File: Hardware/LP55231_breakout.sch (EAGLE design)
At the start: 29 parts, among them J1 To micro, J2 USER LED, J3 USER LED, J4 USER LED, U1 LP55231WQFN

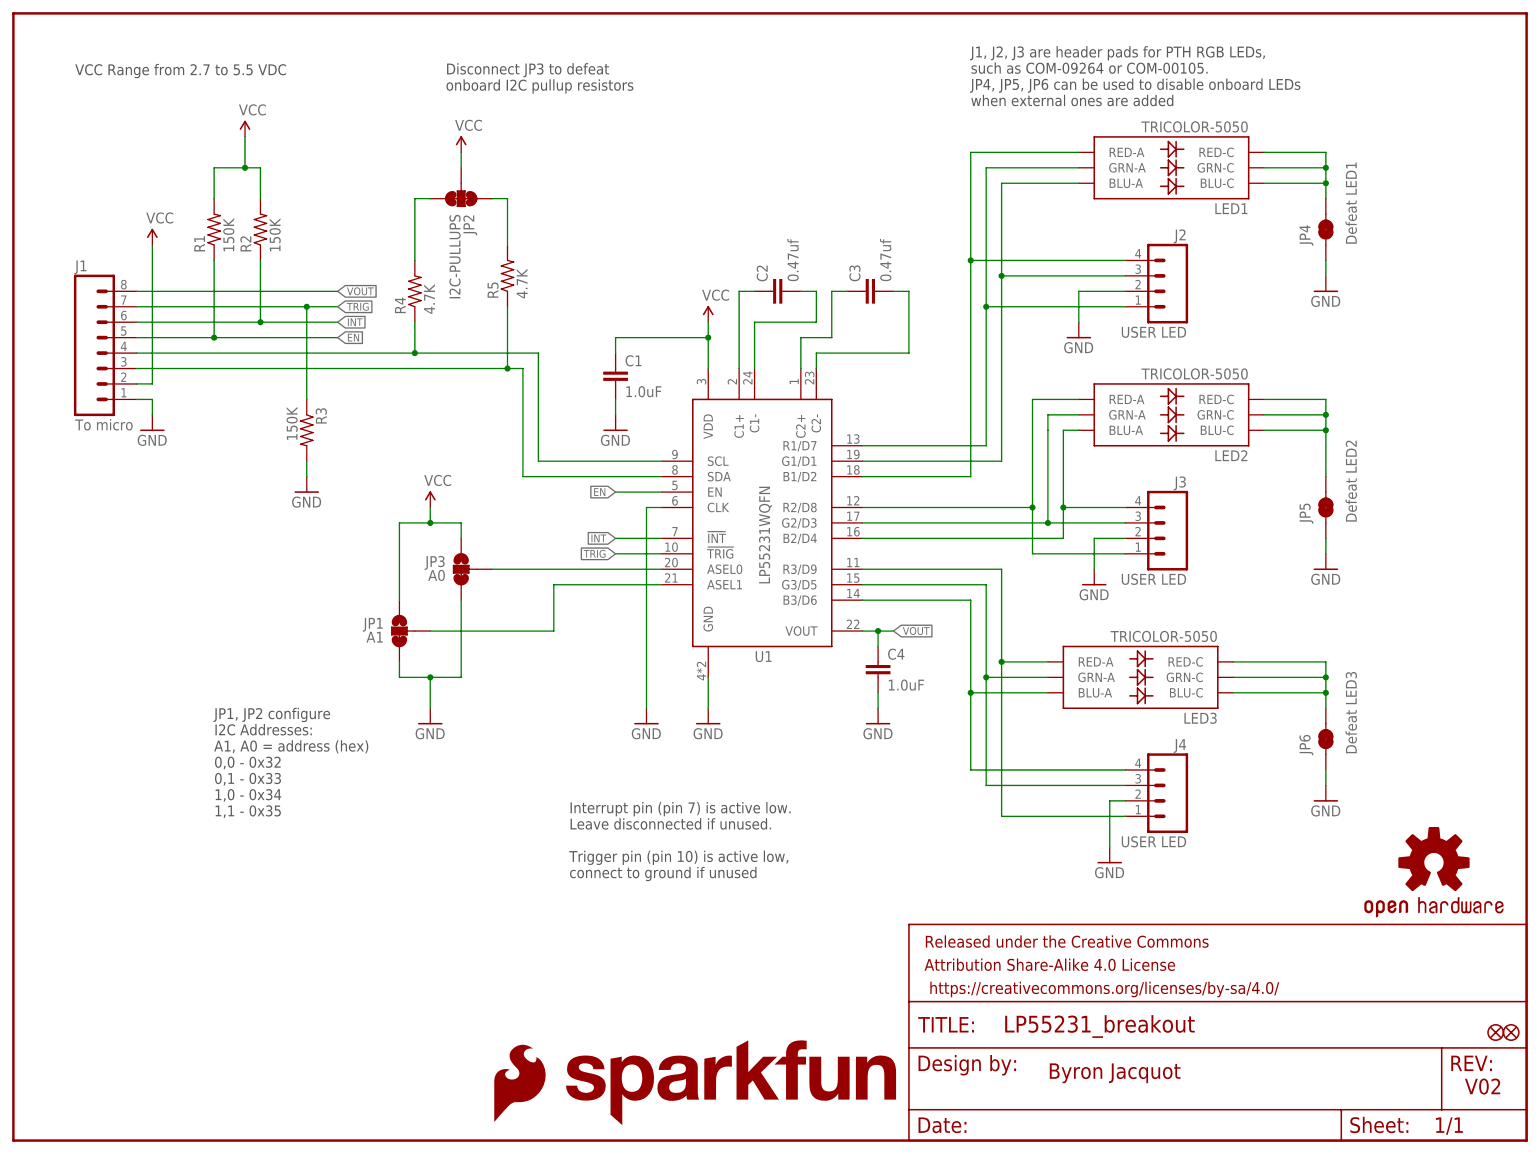
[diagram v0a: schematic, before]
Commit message: Checklist review issues
Numbering of jumpers vs. comments got mismatched.
Now fixed.
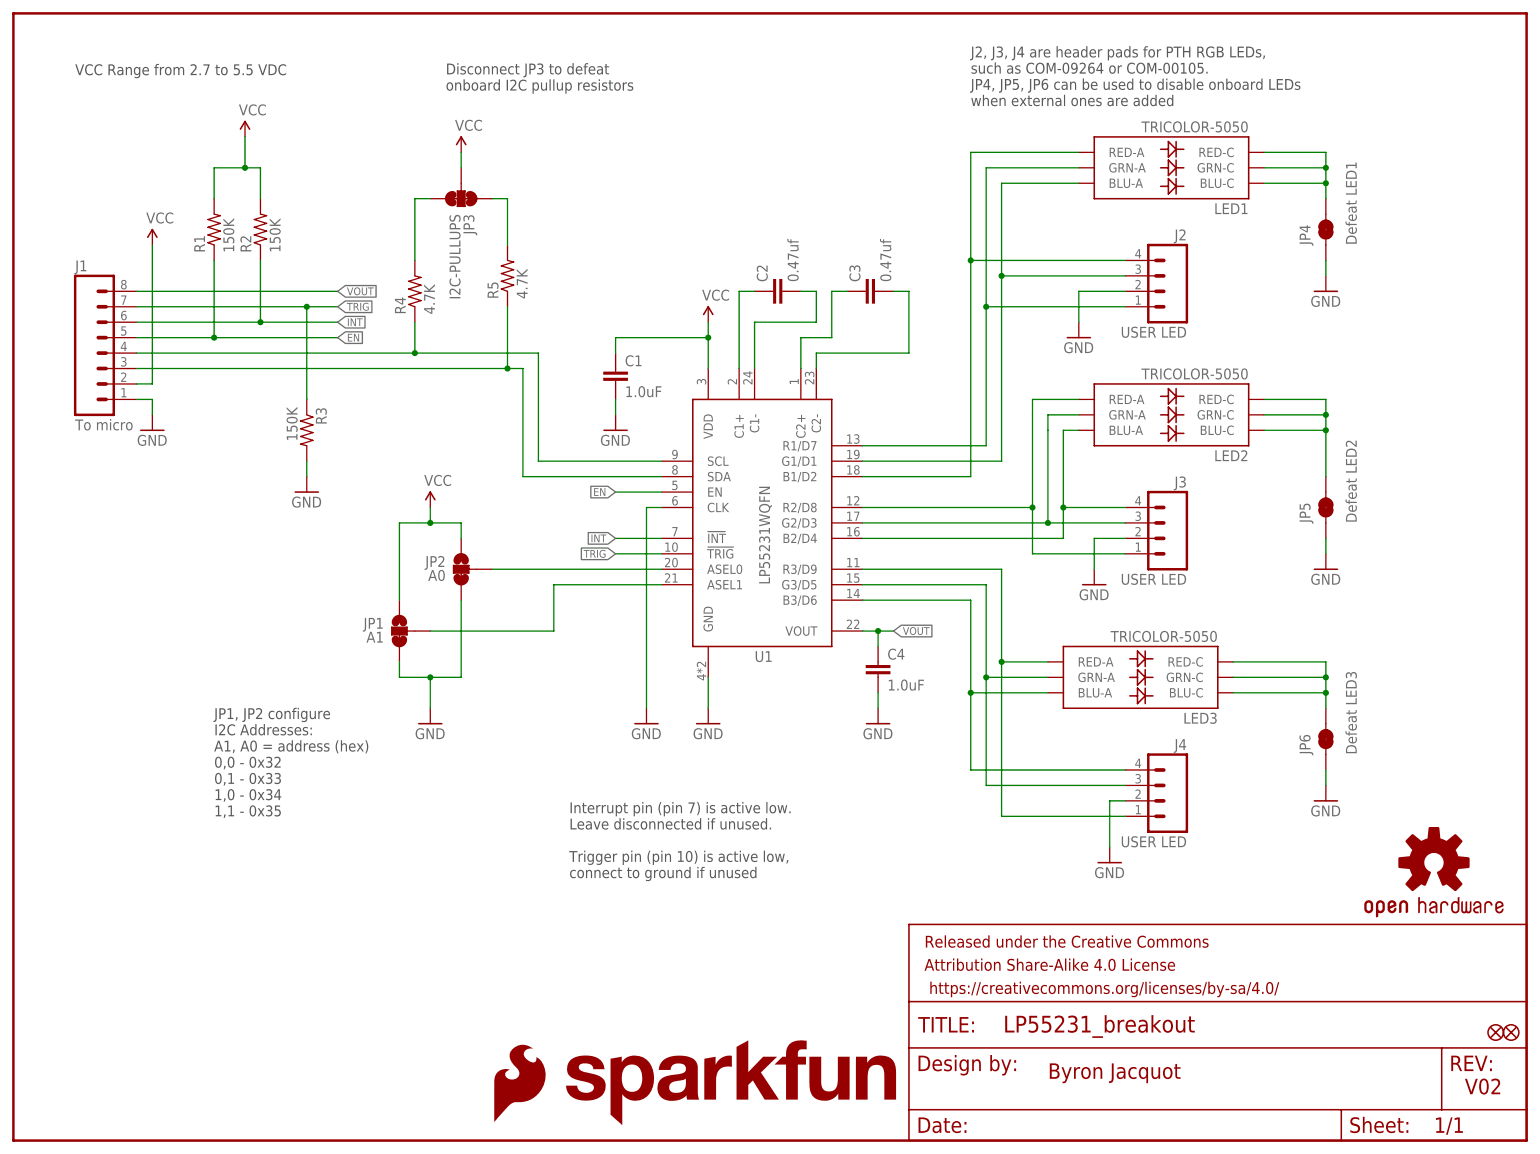
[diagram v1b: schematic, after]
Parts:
- JP2: value I2C-PULLUPS -> A0; device SparkFun-Passives:JUMPER-PAD-3-NC_BY_TRACE -> SparkFun-Passives:JUMPER-PAD-3-2OF3_NC_BY_TRACE_SMALL
- JP3: value A0 -> I2C-PULLUPS; device SparkFun-Passives:JUMPER-PAD-3-2OF3_NC_BY_TRACE_SMALL -> SparkFun-Passives:JUMPER-PAD-3-NC_BY_TRACE
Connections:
- net ADDR0: now also JP2.2; no longer JP3.2
- net GND: now also JP2.3; no longer JP3.3
- net N$21: now also JP3.1; no longer JP2.1
- net N$22: now also JP3.3; no longer JP2.3
- net VCC: now also JP2.1, JP3.2; no longer JP2.2, JP3.1
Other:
- note added: "J2, J3, J4 are header pads for PTH RGB LEDs, such as COM-09264 or COM-00105. JP4, JP5, JP6 can be used to disable onboard LEDs when external ones are added"
- note removed: "J1, J2, J3 are header pads for PTH RGB LEDs, such as COM-09264 or COM-00105. JP4, JP5, JP6 can be used to disable onboard LEDs when external ones are added"
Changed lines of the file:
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@@
 <attribute name="SEE-ALSO" value="battery bayasitter"/>
 </part>
-<part name="JP3" library="SparkFun-Passives" deviceset="JUMPER-PAD-3-2OF3_NC_BY_TRACE" device="_SMALL" value="A0"/>
+<part name="JP2" library="SparkFun-Passives" deviceset="JUMPER-PAD-3-2OF3_NC_BY_TRACE" device="_SMALL" value="A0"/>
 <part name="JP1" library="SparkFun-Passives" deviceset="JUMPER-PAD-3-2OF3_NC_BY_TRACE" device="_SMALL" value="A1"/>
 <part name="GND3" library="SparkFun-Aesthetics" deviceset="GND" device=""/>
@@
 <part name="GND1" library="SparkFun-Aesthetics" deviceset="GND" device=""/>
 <part name="SUPPLY1" library="SparkFun-Aesthetics" deviceset="VCC" device=""/>
-<part name="JP2" library="SparkFun-Passives" deviceset="JUMPER-PAD-3-NC_BY_TRACE" device="" value="I2C-PULLUPS"/>
+<part name="JP3" library="SparkFun-Passives" deviceset="JUMPER-PAD-3-NC_BY_TRACE" device="" value="I2C-PULLUPS"/>
 <part name="SUPPLY4" library="SparkFun-Aesthetics" deviceset="VCC" device=""/>
 <part name="R4" library="SparkFun-Resistors" deviceset="4.7KOHM-1/10W-1%(0603)" device="" value="4.7K"/>
@@
 1,0 - 0x34
 1,1 - 0x35</text>
-<text x="157.48" y="170.18" size="1.778" layer="97" font="vector">J1, J2, J3 are header pads for PTH RGB LEDs,
+<text x="157.48" y="170.18" size="1.778" layer="97" font="vector">J2, J3, J4 are header pads for PTH RGB LEDs,
 such as COM-09264 or COM-00105.
 JP4, JP5, JP6 can be used to disable onboard LEDs
@@
 <attribute name="SEE-ALSO" x="142.24" y="139.7" size="1.778" layer="96" font="vector" rot="R90" display="off"/>
 </instance>
-<instance part="JP3" gate="G$1" x="73.66" y="93.98" rot="MR0"/>
+<instance part="JP2" gate="G$1" x="73.66" y="93.98" rot="MR0"/>
 <instance part="JP1" gate="G$1" x="63.5" y="83.82" rot="MR0"/>
 <instance part="GND3" gate="1" x="68.58" y="68.58"/>
@@
 <instance part="GND1" gate="1" x="22.86" y="116.84"/>
 <instance part="SUPPLY1" gate="G$1" x="22.86" y="147.32"/>
-<instance part="JP2" gate="G$1" x="73.66" y="154.94" rot="R270"/>
+<instance part="JP3" gate="G$1" x="73.66" y="154.94" rot="R270"/>
 <instance part="SUPPLY4" gate="G$1" x="73.66" y="162.56"/>
 <instance part="R4" gate="G$1" x="66.04" y="139.7" rot="R90"/>
@@
 <pinref part="JP1" gate="G$1" pin="3"/>
 <wire x1="63.5" y1="76.2" x2="63.5" y2="78.74" width="0.1524" layer="91"/>
-<pinref part="JP3" gate="G$1" pin="3"/>
+<pinref part="JP2" gate="G$1" pin="3"/>
 <wire x1="73.66" y1="88.9" x2="73.66" y2="76.2" width="0.1524" layer="91"/>
 <wire x1="73.66" y1="76.2" x2="68.58" y2="76.2" width="0.1524" layer="91"/>
@@
 </segment>
 <segment>
-<pinref part="JP3" gate="G$1" pin="1"/>
+<pinref part="JP2" gate="G$1" pin="1"/>
 <wire x1="73.66" y1="99.06" x2="73.66" y2="101.6" width="0.1524" layer="91"/>
 <wire x1="73.66" y1="101.6" x2="68.58" y2="101.6" width="0.1524" layer="91"/>
@@
 <segment>
 <pinref part="SUPPLY4" gate="G$1" pin="VCC"/>
-<pinref part="JP2" gate="G$1" pin="2"/>
+<pinref part="JP3" gate="G$1" pin="2"/>
 <wire x1="73.66" y1="162.56" x2="73.66" y2="160.02" width="0.1524" layer="91"/>
 </segment>
@@
 <segment>
 <pinref part="U1" gate="G$1" pin="ASEL0"/>
-<pinref part="JP3" gate="G$1" pin="2"/>
+<pinref part="JP2" gate="G$1" pin="2"/>
 <wire x1="106.68" y1="93.98" x2="78.74" y2="93.98" width="0.1524" layer="91"/>
 </segment>
@@
 <pinref part="R5" gate="G$1" pin="2"/>
 <wire x1="81.28" y1="147.32" x2="81.28" y2="154.94" width="0.1524" layer="91"/>
-<pinref part="JP2" gate="G$1" pin="1"/>
+<pinref part="JP3" gate="G$1" pin="1"/>
 <wire x1="81.28" y1="154.94" x2="78.74" y2="154.94" width="0.1524" layer="91"/>
 </segment>
@@
 <pinref part="R4" gate="G$1" pin="2"/>
 <wire x1="66.04" y1="144.78" x2="66.04" y2="154.94" width="0.1524" layer="91"/>
-<pinref part="JP2" gate="G$1" pin="3"/>
+<pinref part="JP3" gate="G$1" pin="3"/>
 <wire x1="66.04" y1="154.94" x2="68.58" y2="154.94" width="0.1524" layer="91"/>
 </segment>

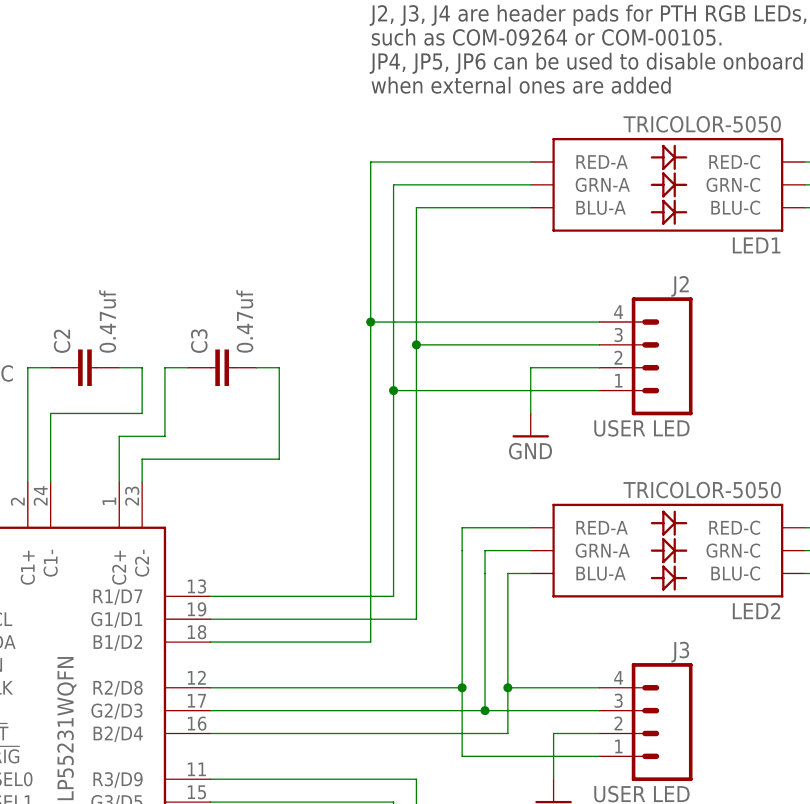
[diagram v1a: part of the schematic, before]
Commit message: Fixing RGB assignments of first LED.
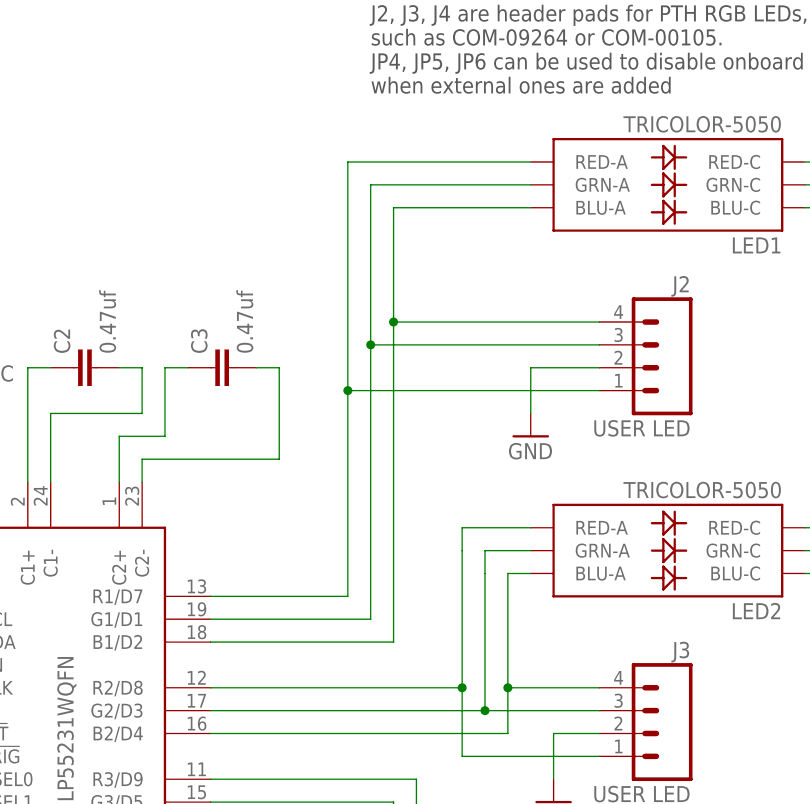
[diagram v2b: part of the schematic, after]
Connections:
- net B1: now also LED1.BLU-A; no longer LED1.RED-A
- net G1: now also LED1.GRN-A; no longer LED1.BLU-A
- net R1: now also LED1.RED-A; no longer LED1.GRN-A
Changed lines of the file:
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@@
 <setting verticaltext="up"/>
 </settings>
-<grid distance="0.1" unitdist="inch" unit="inch" style="lines" multiple="1" display="no" altdistance="0.01" altunitdist="inch" altunit="inch"/>
+<grid distance="0.1" unitdist="inch" unit="inch" style="lines" multiple="1" display="yes" altdistance="0.01" altunitdist="inch" altunit="inch"/>
 <layers>
 <layer number="1" name="Top" color="4" fill="1" visible="no" active="no"/>
@@
 <segment>
 <pinref part="U1" gate="G$1" pin="R1/D7"/>
-<wire x1="139.7" y1="114.3" x2="160.02" y2="114.3" width="0.1524" layer="91"/>
-<wire x1="160.02" y1="114.3" x2="160.02" y2="137.16" width="0.1524" layer="91"/>
-<wire x1="160.02" y1="137.16" x2="160.02" y2="160.02" width="0.1524" layer="91"/>
-<wire x1="160.02" y1="160.02" x2="175.26" y2="160.02" width="0.1524" layer="91"/>
+<wire x1="139.7" y1="114.3" x2="154.94" y2="114.3" width="0.1524" layer="91"/>
+<wire x1="154.94" y1="114.3" x2="154.94" y2="137.16" width="0.1524" layer="91"/>
+<pinref part="LED1" gate="D1" pin="RED-A"/>
+<wire x1="154.94" y1="137.16" x2="154.94" y2="162.56" width="0.1524" layer="91"/>
+<wire x1="154.94" y1="162.56" x2="175.26" y2="162.56" width="0.1524" layer="91"/>
 <pinref part="J2" gate="G$1" pin="1"/>
-<wire x1="182.88" y1="137.16" x2="160.02" y2="137.16" width="0.1524" layer="91"/>
-<junction x="160.02" y="137.16"/>
+<wire x1="182.88" y1="137.16" x2="154.94" y2="137.16" width="0.1524" layer="91"/>
+<junction x="154.94" y="137.16"/>
+</segment>
+</net>
+<net name="G1" class="0">
+<segment>
+<pinref part="U1" gate="G$1" pin="G1/D1"/>
+<wire x1="139.7" y1="111.76" x2="157.48" y2="111.76" width="0.1524" layer="91"/>
+<wire x1="157.48" y1="111.76" x2="157.48" y2="142.24" width="0.1524" layer="91"/>
 <pinref part="LED1" gate="D1" pin="GRN-A"/>
-</segment>
-</net>
-<net name="G1" class="0">
-<segment>
-<pinref part="U1" gate="G$1" pin="G1/D1"/>
-<wire x1="139.7" y1="111.76" x2="162.56" y2="111.76" width="0.1524" layer="91"/>
-<wire x1="162.56" y1="111.76" x2="162.56" y2="142.24" width="0.1524" layer="91"/>
-<wire x1="162.56" y1="142.24" x2="162.56" y2="157.48" width="0.1524" layer="91"/>
-<wire x1="162.56" y1="157.48" x2="175.26" y2="157.48" width="0.1524" layer="91"/>
+<wire x1="157.48" y1="142.24" x2="157.48" y2="160.02" width="0.1524" layer="91"/>
+<wire x1="157.48" y1="160.02" x2="175.26" y2="160.02" width="0.1524" layer="91"/>
 <pinref part="J2" gate="G$1" pin="3"/>
-<wire x1="182.88" y1="142.24" x2="162.56" y2="142.24" width="0.1524" layer="91"/>
-<junction x="162.56" y="142.24"/>
+<wire x1="182.88" y1="142.24" x2="157.48" y2="142.24" width="0.1524" layer="91"/>
+<junction x="157.48" y="142.24"/>
+</segment>
+</net>
+<net name="B1" class="0">
+<segment>
+<pinref part="U1" gate="G$1" pin="B1/D2"/>
+<wire x1="139.7" y1="109.22" x2="160.02" y2="109.22" width="0.1524" layer="91"/>
+<wire x1="160.02" y1="109.22" x2="160.02" y2="144.78" width="0.1524" layer="91"/>
 <pinref part="LED1" gate="D1" pin="BLU-A"/>
-</segment>
-</net>
-<net name="B1" class="0">
-<segment>
-<pinref part="U1" gate="G$1" pin="B1/D2"/>
-<wire x1="139.7" y1="109.22" x2="157.48" y2="109.22" width="0.1524" layer="91"/>
-<wire x1="157.48" y1="109.22" x2="157.48" y2="144.78" width="0.1524" layer="91"/>
-<wire x1="157.48" y1="144.78" x2="157.48" y2="162.56" width="0.1524" layer="91"/>
-<wire x1="157.48" y1="162.56" x2="175.26" y2="162.56" width="0.1524" layer="91"/>
+<wire x1="160.02" y1="144.78" x2="160.02" y2="157.48" width="0.1524" layer="91"/>
+<wire x1="160.02" y1="157.48" x2="175.26" y2="157.48" width="0.1524" layer="91"/>
 <pinref part="J2" gate="G$1" pin="4"/>
-<wire x1="182.88" y1="144.78" x2="157.48" y2="144.78" width="0.1524" layer="91"/>
-<junction x="157.48" y="144.78"/>
-<pinref part="LED1" gate="D1" pin="RED-A"/>
-</segment>
-</net>
+<wire x1="182.88" y1="144.78" x2="160.02" y2="144.78" width="0.1524" layer="91"/>
+<junction x="160.02" y="144.78"/>
+</segment>
+</net>

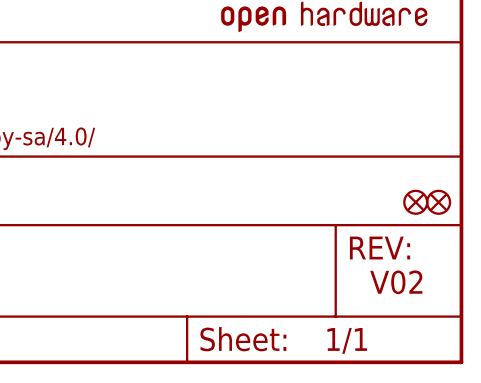
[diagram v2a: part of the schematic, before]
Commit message: Rolling version number
From V02 to V03.
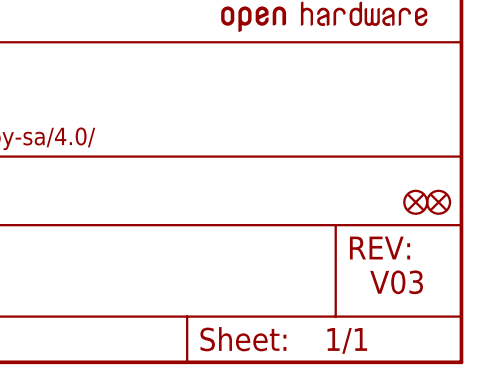
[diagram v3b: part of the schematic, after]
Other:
- note added: "V03"
- note removed: "V02"
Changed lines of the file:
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@@
 <setting verticaltext="up"/>
 </settings>
-<grid distance="0.1" unitdist="inch" unit="inch" style="lines" multiple="1" display="yes" altdistance="0.01" altunitdist="inch" altunit="inch"/>
+<grid distance="0.1" unitdist="inch" unit="inch" style="lines" multiple="1" display="no" altdistance="0.01" altunitdist="inch" altunit="inch"/>
 <layers>
 <layer number="1" name="Top" color="4" fill="1" visible="no" active="no"/>
@@
 <plain>
 <text x="170.18" y="10.16" size="2.54" layer="94" font="vector">Byron Jacquot</text>
-<text x="238.76" y="7.62" size="2.54" layer="94" font="vector">V02</text>
+<text x="238.76" y="7.62" size="2.54" layer="94" font="vector">V03</text>
 <text x="10.16" y="175.26" size="1.778" layer="97" font="vector">VCC Range from 2.7 to 5.5 VDC</text>
 <text x="33.02" y="53.34" size="1.778" layer="97" font="vector">JP1, JP2 configure
